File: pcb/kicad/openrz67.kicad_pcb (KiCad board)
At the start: 2 copper layers, 48 x 22 mm, 59 parts, among them U1 ESP32-C3FH4, U3 LGS5500EP, U4 S4B-XH-A(LF)(SN), U5 TLP172GM, U6 TLP172GM, X1 40MHz, X2 32.768kHz

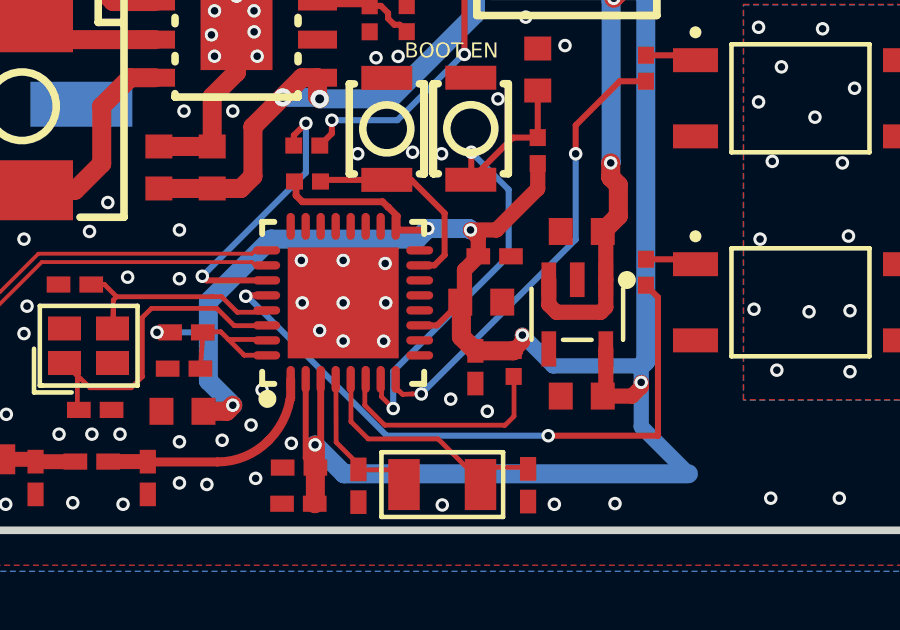
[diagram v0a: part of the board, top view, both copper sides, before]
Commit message: Review follow-ups: S1 driver to GPIO4, 220 R LED resistors, S1_DRV/S2_DRV nets
GPIO21 is U0TXD and idles high from the ROM boot log until setup() runs, so
the S1 output was closed during every boot. Harmless on its own, since the
camera needs S1 and S2 together, but GPIO4 (U1 pin 9, free) is a plain input
at reset, and the move frees UART0 TX for logging. Firmware constants
renamed to shutterPinS1 = 4 / shutterPinS2 = 3; builds.

330 R gave 3.8 mA at worst-case VOH/VF, under Toshiba's 5 mA minimum; 220 R
(C25091, Basic) gives 5.6 mA worst case, 9 mA typical.

Nets D6/D1 (Wemos names) renamed S1_DRV/S2_DRV. The S2_DRV bottom-layer
diagonal moved 0.3 mm to make room for the new via next to U1 pin 10.

DRC 0 errors / 7 known warnings, ERC 0/0, parity clean.
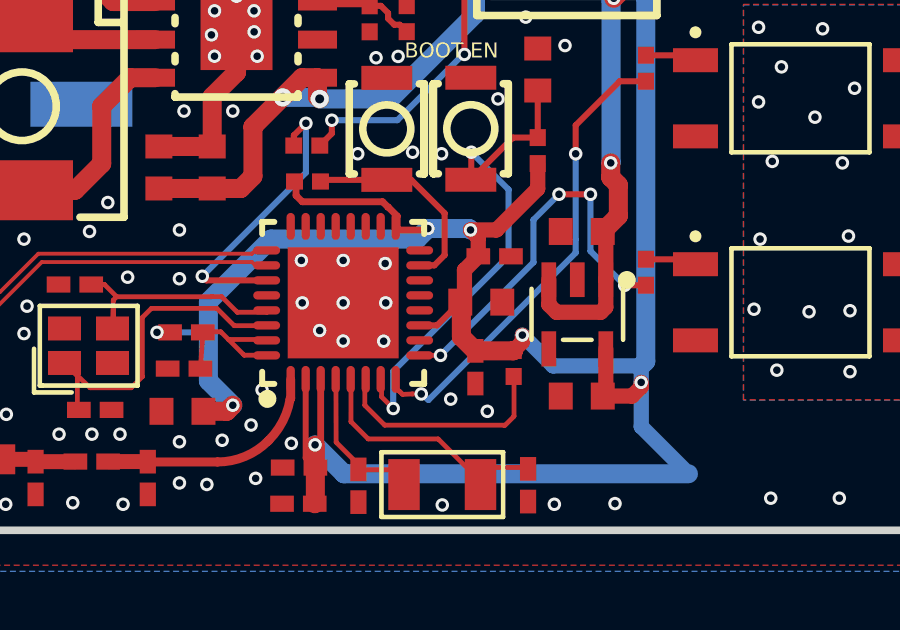
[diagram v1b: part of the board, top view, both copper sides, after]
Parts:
- R21, R22: value 330Ω -> 220Ω
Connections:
- net D1 renamed S2_DRV
- R21 pad 2: D6 -> S1_DRV
- U1 pad 28: D6 -> unconnected-(U1-U0TXD-Pad28)
- U1 pad 9: unconnected-(U1-MTMS-Pad9) -> S1_DRV
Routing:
- net D6: track 21.7 -> 0.00 mm, vias 2 -> 0
- net S1_DRV: track 0.00 -> 13.0 mm, vias 0 -> 4
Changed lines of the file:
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@@
 			)
 		)
-		(property "Value" "330Ω"
+		(property "Value" "220Ω"
 			(at 0 0 270)
 			(layer "F.Fab")
@@
 			)
 		)
-		(property "Datasheet" "https://www.lcsc.com/product-detail/C25104.html"
+		(property "Datasheet" "https://www.lcsc.com/product-detail/C25091.html"
 			(at 0 0 270)
 			(layer "F.Fab")
@@
 			)
 		)
-		(property "Manufacturer Part" "0402WGF3300TCE"
+		(property "Manufacturer Part" "0402WGF2200TCE"
 			(at 0 0 0)
 			(layer "F.Fab")
@@
 			)
 		)
-		(property "Supplier Part" "C25104"
+		(property "Supplier Part" "C25091"
 			(at 0 0 0)
 			(layer "F.Fab")
@@
 			)
 		)
-		(property "LCSC Part Name" "330Ω ±1% 62.5mW 厚膜电阻"
+		(property "LCSC Part Name" "220Ω ±1% 62.5mW 厚膜电阻"
 			(at 0 0 0)
 			(layer "F.Fab")
@@
 			(size 0.5655 0.54)
 			(layers "F.Cu" "F.Mask" "F.Paste")
-			(net "D6")
+			(net "S1_DRV")
 		)
 		(embedded_fonts no)
@@
 			(size 0.28 0.9)
 			(layers "F.Cu" "F.Mask" "F.Paste")
-			(net "D1")
+			(net "S2_DRV")
 		)
 		(pad "9" smd oval
@@
 			(size 0.9 0.28)
 			(layers "F.Cu" "F.Mask" "F.Paste")
-			(net "unconnected-(U1-MTMS-Pad9)")
+			(net "S1_DRV")
 		)
 		(pad "10" smd oval
@@
 			(size 0.9 0.28)
 			(layers "F.Cu" "F.Mask" "F.Paste")
-			(net "D6")
+			(net "unconnected-(U1-U0TXD-Pad28)")
 		)
 		(pad "29" smd oval
@@
 			)
 		)
-		(property "Value" "330Ω"
+		(property "Value" "220Ω"
 			(at 0 0 270)
 			(layer "F.Fab")
@@
 			)
 		)
-		(property "Datasheet" "https://www.lcsc.com/product-detail/C25104.html"
+		(property "Datasheet" "https://www.lcsc.com/product-detail/C25091.html"
 			(at 0 0 270)
 			(layer "F.Fab")
@@
 			)
 		)
-		(property "Manufacturer Part" "0402WGF3300TCE"
+		(property "Manufacturer Part" "0402WGF2200TCE"
 			(at 0 0 0)
 			(layer "F.Fab")
@@
 			)
 		)
-		(property "Supplier Part" "C25104"
+		(property "Supplier Part" "C25091"
 			(at 0 0 0)
 			(layer "F.Fab")
@@
 			)
 		)
-		(property "LCSC Part Name" "330Ω ±1% 62.5mW 厚膜电阻"
+		(property "LCSC Part Name" "220Ω ±1% 62.5mW 厚膜电阻"
 			(at 0 0 0)
 			(layer "F.Fab")
@@
 			(size 0.5655 0.54)
 			(layers "F.Cu" "F.Mask" "F.Paste")
-			(net "D1")
+			(net "S2_DRV")
 		)
 		(embedded_fonts no)
@@
 	)
 	(segment
-		(start 138.7795 104.1695)
-		(end 138.0375 104.1695)
-		(width 0.203)
+		(start 143.807 106.1695)
+		(end 144.5 106.1695)
+		(width 0.16)
 		(layer "F.Cu")
-		(net "D6")
+		(net "S1_DRV")
 	)
 	(segment
-		(start 138.0375 104.1695)
-		(end 137.983 104.224)
+		(start 150.64 103.833)
+		(end 151.35 103.833)
 		(width 0.203)
 		(layer "F.Cu")
-		(net "D6")
+		(net "S1_DRV")
 	)
 	(segment
-		(start 151.75 108.847)
-		(end 151.75 104.233)
+		(start 148.45 100.8)
+		(end 149.5 100.8)
 		(width 0.203)
 		(layer "F.Cu")
-		(net "D6")
+		(net "S1_DRV")
 	)
-	(segment
-		(start 151.75 104.233)
-		(end 151.35 103.833)
-		(width 0.203)
-		(layer "F.Cu")
-		(net "D6")
+	(via
+		(at 144.5 106.1695)
+		(size 0.45)
+		(drill 0.25)
+		(layers "F.Cu" "B.Cu")
+		(net "S1_DRV")
 	)
-	(segment
-		(start 148.0925 108.847)
-		(end 151.75 108.847)
-		(width 0.203)
-		(layer "F.Cu")
-		(net "D6")
+	(via
+		(at 148.45 100.8)
+		(size 0.45)
+		(drill 0.25)
+		(layers "F.Cu" "B.Cu")
+		(net "S1_DRV")
 	)
 	(via
-		(at 148.0925 108.847)
+		(at 150.64 103.833)
 		(size 0.45)
 		(drill 0.25)
 		(layers "F.Cu" "B.Cu")
-		(net "D6")
+		(net "S1_DRV")
 	)
 	(via
-		(at 138.0085 104.1985)
+		(at 149.5 100.8)
 		(size 0.45)
 		(drill 0.25)
 		(layers "F.Cu" "B.Cu")
-		(net "D6")
+		(net "S1_DRV")
+	)
+	(segment
+		(start 149.5 102.693)
+		(end 150.64 103.833)
+		(width 0.203)
+		(layer "B.Cu")
+		(net "S1_DRV")
+	)
+	(segment
+		(start 147.6 103.0695)
+		(end 147.6 101.65)
+		(width 0.203)
+		(layer "B.Cu")
+		(net "S1_DRV")
 	)
 	(segment
-		(start 148.0925 108.847)
-		(end 142.7075 108.847)
+		(start 147.6 101.65)
+		(end 148.45 100.8)
 		(width 0.203)
 		(layer "B.Cu")
-		(net "D6")
+		(net "S1_DRV")
 	)
 	(segment
-		(start 142.7075 108.847)
-		(end 138.0595 104.1985)
+		(start 144.5 106.1695)
+		(end 147.6 103.0695)
 		(width 0.203)
 		(layer "B.Cu")
-		(net "D6")
+		(net "S1_DRV")
 	)
 	(segment
-		(start 138.0595 104.1985)
-		(end 138.0085 104.1985)
+		(start 149.5 100.8)
+		(end 149.5 102.693)
 		(width 0.203)
 		(layer "B.Cu")
-		(net "D6")
+		(net "S1_DRV")
 	)
 	(segment
@@
 		(width 0.203)
 		(layer "F.Cu")
-		(net "D1")
+		(net "S2_DRV")
 	)
 	(segment
@@
 		(width 0.16)
 		(layer "F.Cu")
-		(net "D1")
+		(net "S2_DRV")
 	)
 	(segment
@@
 		(width 0.16)
 		(layer "F.Cu")
-		(net "D1")
+		(net "S2_DRV")
 	)
 	(segment
@@
 		(width 0.16)
 		(layer "F.Cu")
-		(net "D1")
+		(net "S2_DRV")
 	)
 	(segment
@@
 		(width 0.16)
 		(layer "F.Cu")
-		(net "D1")
+		(net "S2_DRV")
 	)
 	(segment
@@
 		(width 0.16)
 		(layer "F.Cu")
-		(net "D1")
+		(net "S2_DRV")
 	)
 	(segment
@@
 		(width 0.16)
 		(layer "F.Cu")
-		(net "D1")
+		(net "S2_DRV")
 	)
 	(segment
@@
 		(width 0.16)
 		(layer "F.Cu")
-		(net "D1")
+		(net "S2_DRV")
 	)
 	(segment
@@
 		(width 0.16)
 		(layer "F.Cu")
-		(net "D1")
+		(net "S2_DRV")
 	)
 	(segment
@@
 		(width 0.203)
 		(layer "F.Cu")
-		(net "D1")
+		(net "S2_DRV")
 	)
 	(segment
@@
 		(width 0.203)
 		(layer "F.Cu")
-		(net "D1")
+		(net "S2_DRV")
 	)
 	(via
@@
 		(drill 0.25)
 		(layers "F.Cu" "B.Cu")
-		(net "D1")
+		(net "S2_DRV")
 	)
 	(via
@@
 		(drill 0.25)
 		(layers "F.Cu" "B.Cu")
-		(net "D1")
+		(net "S2_DRV")
 	)
 	(segment
@@
 		(width 0.203)
 		(layer "B.Cu")
-		(net "D1")
+		(net "S2_DRV")
 	)
 	(segment
 		(start 149.007 102.3085)
+		(end 149.007 102.75)
+		(width 0.203)
+		(layer "B.Cu")
+		(net "S2_DRV")
+	)
+	(segment
+		(start 144.1 107.657)
 		(end 143.86 107.4555)
 		(width 0.203)
 		(layer "B.Cu")
-		(net "D1")
+		(net "S2_DRV")
+	)
+	(segment
+		(start 149.007 102.75)
+		(end 144.1 107.657)
+		(width 0.203)
+		(layer "B.Cu")
+		(net "S2_DRV")
 	)
 	(segment

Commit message: Use lower-resistance PhotoMOS relays
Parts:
- U5, U6: value TLP172GM -> TLP172AM
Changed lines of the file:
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@@
 			)
 		)
-		(property "Value" "TLP172GM"
+		(property "Value" "TLP172AM"
 			(at 0 0 180)
 			(layer "F.Fab")
@@
 			)
 		)
-		(property "Datasheet" "https://toshiba.semicon-storage.com/info/TLP172GM_datasheet_en_20230525.pdf"
+		(property "Datasheet" "https://toshiba.semicon-storage.com/info/docget.jsp?did=36714&prodName=TLP172AM"
 			(at 0 0 180)
 			(layer "F.Fab")
@@
 			)
 		)
-		(property "Description" "PhotoMOS relay, 1-Form-A, 350 V / 110 mA, 4-pin SO6"
+		(property "Description" "PhotoMOS relay, 1-Form-A, 60 V / 500 mA, 4-pin SO6"
 			(at 0 0 180)
 			(layer "F.Fab")
@@
 			)
 		)
-		(property "Manufacturer Part" "TLP172GM(TPL,E"
+		(property "Manufacturer Part" "TLP172AM(TPL,E"
 			(at 0 0 180)
 			(layer "F.Fab")
@@
 			)
 		)
-		(property "Supplier Part" "C261926"
+		(property "Supplier Part" "C2152276"
 			(at 0 0 180)
 			(layer "F.Fab")
@@
 			)
 		)
-		(property "LCSC Part Name" "TLP172GM(TPL,E"
+		(property "LCSC Part Name" "TLP172AM(TPL,E"
 			(at 0 0 180)
 			(layer "F.Fab")
@@
 			)
 		)
-		(property "Value" "TLP172GM"
+		(property "Value" "TLP172AM"
 			(at 0 0 180)
 			(layer "F.Fab")
@@
 			)
 		)
-		(property "Datasheet" "https://toshiba.semicon-storage.com/info/TLP172GM_datasheet_en_20230525.pdf"
+		(property "Datasheet" "https://toshiba.semicon-storage.com/info/docget.jsp?did=36714&prodName=TLP172AM"
 			(at 0 0 180)
 			(layer "F.Fab")
@@
 			)
 		)
-		(property "Description" "PhotoMOS relay, 1-Form-A, 350 V / 110 mA, 4-pin SO6"
+		(property "Description" "PhotoMOS relay, 1-Form-A, 60 V / 500 mA, 4-pin SO6"
 			(at 0 0 180)
 			(layer "F.Fab")
@@
 			)
 		)
-		(property "Manufacturer Part" "TLP172GM(TPL,E"
+		(property "Manufacturer Part" "TLP172AM(TPL,E"
 			(at 0 0 180)
 			(layer "F.Fab")
@@
 			)
 		)
-		(property "Supplier Part" "C261926"
+		(property "Supplier Part" "C2152276"
 			(at 0 0 180)
 			(layer "F.Fab")
@@
 			)
 		)
-		(property "LCSC Part Name" "TLP172GM(TPL,E"
+		(property "LCSC Part Name" "TLP172AM(TPL,E"
 			(at 0 0 180)
 			(layer "F.Fab")

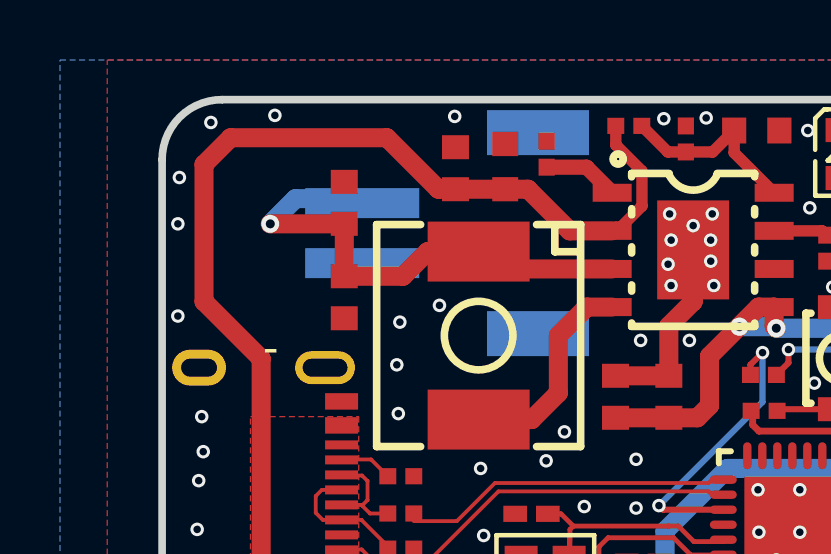
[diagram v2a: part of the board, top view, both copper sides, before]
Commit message: Move battery connector back to top
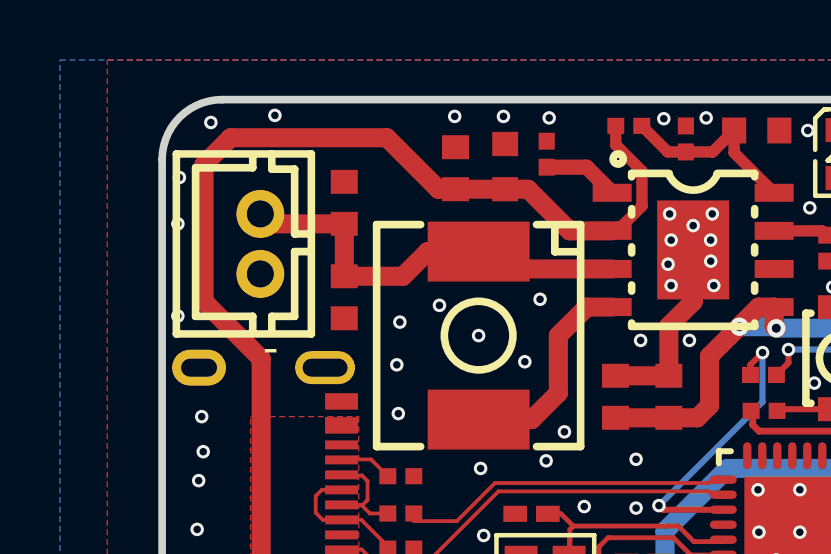
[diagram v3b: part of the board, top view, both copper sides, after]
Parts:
- BAT1: value S2B-PH-SM4-TB(LF)(SN) -> B2B-PH-K-S(LF)(SN); footprint openrz67:CONN-SMD_P2.00_S2B-PH-SM4-TB-LF-SN -> openrz67:CONN-TH_B2B-PH-K-S; moved to F.Cu
- moved BAT1 6.34 mm to (123.3, 94.8), turned to 90 degrees
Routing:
- net BAT+: track 17.1 -> 14.2 mm, vias 1 -> 0
- net GND: vias 103 -> 108
